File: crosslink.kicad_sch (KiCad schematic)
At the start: 32 parts, among them U16 CrossLink_LIF-MD6000-6JMG80I

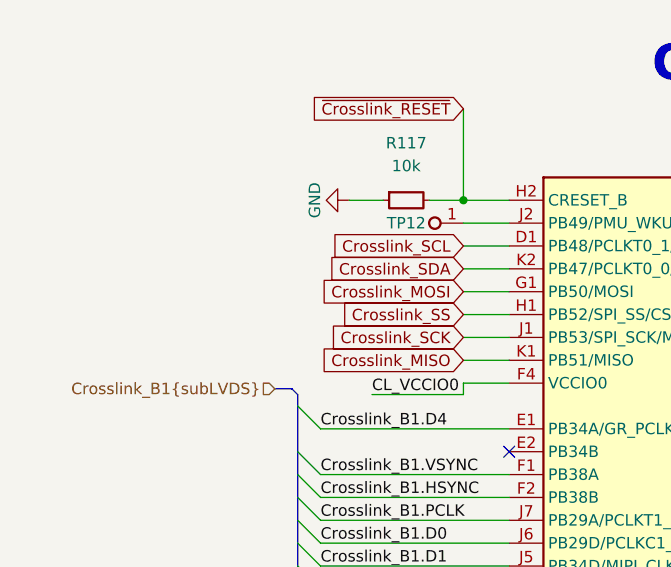
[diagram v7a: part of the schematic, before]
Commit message: [#57505] Start moving logic level converters to GPIO sheet
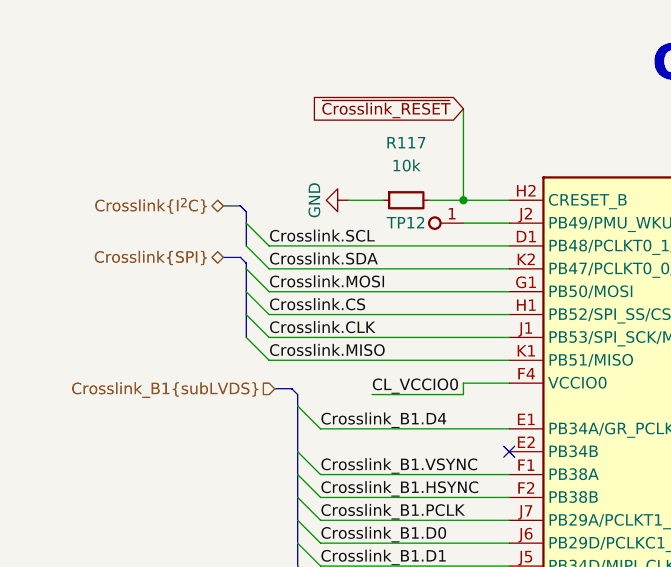
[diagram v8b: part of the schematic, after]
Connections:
- net Crosslink_MISO renamed Crosslink.MISO
- net Crosslink_MOSI renamed Crosslink.MOSI
- net Crosslink_SCK renamed Crosslink.CLK
- net Crosslink_SCL renamed Crosslink.SCL
- net Crosslink_SDA renamed Crosslink.SDA
- net Crosslink_SS renamed Crosslink.CS
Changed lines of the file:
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@@
     (stroke (width 0) (type default))
   )
+  (bus_entry (at 39.37 90.805) (size -2.54 -2.54)
+    (stroke (width 0) (type default))
+  )
   (bus_entry (at 42.545 141.605) (size 2.54 2.54)
     (stroke (width 0) (type default))
@@
     (stroke (width 0) (type default))
   )
+  (bus_entry (at 39.37 103.505) (size -2.54 -2.54)
+    (stroke (width 0) (type default))
+  )
   (bus_entry (at 149.225 139.065) (size -2.54 2.54)
     (stroke (width 0) (type default))
@@
     (stroke (width 0) (type default))
   )
+  (bus_entry (at 39.37 100.965) (size -2.54 -2.54)
+    (stroke (width 0) (type default))
+  )
   (bus_entry (at 149.225 136.525) (size -2.54 2.54)
     (stroke (width 0) (type default))
@@
     (stroke (width 0) (type default))
   )
+  (bus_entry (at 39.37 98.425) (size -2.54 -2.54)
+    (stroke (width 0) (type default))
+  )
   (bus_entry (at 149.225 156.845) (size -2.54 2.54)
     (stroke (width 0) (type default))
@@
     (stroke (width 0) (type default))
   )
+  (bus_entry (at 39.37 95.885) (size -2.54 -2.54)
+    (stroke (width 0) (type default))
+  )
   (bus_entry (at 42.545 116.205) (size 2.54 2.54)
     (stroke (width 0) (type default))
@@
     (stroke (width 0) (type default))
   )
+  (bus_entry (at 39.37 93.345) (size -2.54 -2.54)
+    (stroke (width 0) (type default))
+  )
   (bus_entry (at 42.545 184.785) (size 2.54 2.54)
     (stroke (width 0) (type default))
@@
     (stroke (width 0) (type default))
   )
-  (wire (pts (xy 60.96 93.345) (xy 66.04 93.345))
+  (wire (pts (xy 39.37 93.345) (xy 66.04 93.345))
+    (stroke (width 0) (type default))
+  )
+  (bus (pts (xy 36.83 98.425) (xy 36.83 100.965))
     (stroke (width 0) (type default))
   )
@@
     (stroke (width 0) (type default))
   )
+  (bus (pts (xy 36.83 95.885) (xy 36.83 98.425))
+    (stroke (width 0) (type default))
+  )
   (wire (pts (xy 129.54 111.125) (xy 146.685 111.125))
     (stroke (width 0) (type default))
@@
     (stroke (width 0) (type default))
   )
+  (bus (pts (xy 36.83 88.265) (xy 36.83 90.805))
+    (stroke (width 0) (type default))
+  )
   (wire (pts (xy 304.8 101.6) (xy 311.15 101.6))
     (stroke (width 0) (type default))
@@
     (stroke (width 0) (type default))
   )
-  (wire (pts (xy 60.96 103.505) (xy 66.04 103.505))
+  (wire (pts (xy 39.37 103.505) (xy 66.04 103.505))
     (stroke (width 0) (type default))
   )
@@
     (stroke (width 0) (type default))
   )
+  (bus (pts (xy 34.29 86.36) (xy 36.195 86.36))
+    (stroke (width 0) (type default))
+  )
+  (bus (pts (xy 36.195 92.075) (xy 36.83 92.71))
+    (stroke (width 0) (type default))
+  )
+  (bus (pts (xy 36.195 86.36) (xy 36.83 86.995))
+    (stroke (width 0) (type default))
+  )
   (bus (pts (xy 149.86 133.35) (xy 149.225 133.985))
     (stroke (width 0) (type default))
@@
     (stroke (width 0) (type default))
   )
+  (bus (pts (xy 36.83 86.995) (xy 36.83 88.265))
+    (stroke (width 0) (type default))
+  )
   (wire (pts (xy 45.085 118.745) (xy 66.04 118.745))
     (stroke (width 0) (type default))
@@
     (stroke (width 0) (type default))
   )
-  (wire (pts (xy 60.96 95.885) (xy 66.04 95.885))
+  (wire (pts (xy 39.37 95.885) (xy 66.04 95.885))
     (stroke (width 0) (type default))
   )
@@
     (stroke (width 0) (type default))
   )
-  (wire (pts (xy 60.96 98.425) (xy 66.04 98.425))
+  (wire (pts (xy 39.37 98.425) (xy 66.04 98.425))
     (stroke (width 0) (type default))
   )
@@
     (stroke (width 0) (type default))
   )
-  (wire (pts (xy 60.96 90.805) (xy 66.04 90.805))
+  (wire (pts (xy 39.37 90.805) (xy 66.04 90.805))
     (stroke (width 0) (type default))
   )
@@
     (stroke (width 0) (type default))
   )
+  (bus (pts (xy 36.83 92.71) (xy 36.83 93.345))
+    (stroke (width 0) (type default))
+  )
+  (bus (pts (xy 34.29 92.075) (xy 36.195 92.075))
+    (stroke (width 0) (type default))
+  )
   (bus (pts (xy 149.225 113.665) (xy 149.225 116.205))
     (stroke (width 0) (type default))
@@
     (stroke (width 0) (type default))
   )
+  (bus (pts (xy 36.83 93.345) (xy 36.83 95.885))
+    (stroke (width 0) (type default))
+  )
   (wire (pts (xy 345.44 93.98) (xy 355.6 93.98))
     (stroke (width 0) (type default))
@@
     (stroke (width 0) (type default))
   )
-  (wire (pts (xy 60.96 100.965) (xy 66.04 100.965))
+  (wire (pts (xy 39.37 100.965) (xy 66.04 100.965))
     (stroke (width 0) (type default))
   )
@@
     (effects (font (size 1.27 1.27)) (justify right bottom))
   )
+  (label "Crosslink.CS" (at 39.37 98.425 0) (fields_autoplaced)
+    (effects (font (size 1.27 1.27)) (justify left bottom))
+  )
   (label "Crosslink_B2.D8" (at 45.085 189.865 0) (fields_autoplaced)
     (effects (font (size 1.27 1.27)) (justify left bottom))
@@
     (effects (font (size 1.27 1.27)) (justify right bottom))
   )
+  (label "Crosslink.SDA" (at 39.37 93.345 0) (fields_autoplaced)
+    (effects (font (size 1.27 1.27)) (justify left bottom))
+  )
   (label "DSI1.D2_N" (at 145.415 156.845 180) (fields_autoplaced)
     (effects (font (size 1.27 1.27)) (justify right bottom))
@@
     (effects (font (size 1.27 1.27)) (justify left bottom))
   )
+  (label "Crosslink.MISO" (at 39.37 103.505 0) (fields_autoplaced)
+    (effects (font (size 1.27 1.27)) (justify left bottom))
+  )
   (label "CAM1.C_N" (at 145.415 103.505 180) (fields_autoplaced)
     (effects (font (size 1.27 1.27)) (justify right bottom))
@@
     (effects (font (size 1.27 1.27)) (justify right bottom))
   )
+  (label "Crosslink.SCL" (at 39.37 90.805 0) (fields_autoplaced)
+    (effects (font (size 1.27 1.27)) (justify left bottom))
+  )
   (label "DSI1.C_N" (at 145.415 141.605 180) (fields_autoplaced)
     (effects (font (size 1.27 1.27)) (justify right bottom))
   )
+  (label "Crosslink.MOSI" (at 39.37 95.885 0) (fields_autoplaced)
+    (effects (font (size 1.27 1.27)) (justify left bottom))
+  )
   (label "Crosslink_B1.D9" (at 45.085 144.145 0) (fields_autoplaced)
     (effects (font (size 1.27 1.27)) (justify left bottom))
@@
     (effects (font (size 1.27 1.27)) (justify left bottom))
   )
+  (label "Crosslink.CLK" (at 39.37 100.965 0) (fields_autoplaced)
+    (effects (font (size 1.27 1.27)) (justify left bottom))
+  )
   (label "Crosslink_B1.D4" (at 45.085 111.125 0) (fields_autoplaced)
     (effects (font (size 1.27 1.27)) (justify left bottom))
@@
     (effects (font (size 1.27 1.27)) (justify right bottom))
   )
-  (global_label "Crosslink_SCL" (shape input) (at 60.96 90.805 180) (fields_autoplaced)
-    (effects (font (size 1.27 1.27)) (justify right))
-    (property "Intersheetrefs" "${INTERSHEET_REFS}" (at 45.3631 90.7256 0)
-      (effects (font (size 1.27 1.27)) (justify right))
-    )
-  )
-  (global_label "Crosslink_SCK" (shape input) (at 60.96 100.965 180) (fields_autoplaced)
-    (effects (font (size 1.27 1.27)) (justify right))
-    (property "Intersheetrefs" "${INTERSHEET_REFS}" (at 45.1212 100.8856 0)
-      (effects (font (size 1.27 1.27)) (justify right))
-    )
-  )
-  (global_label "Crosslink_SDA" (shape input) (at 60.96 93.345 180) (fields_autoplaced)
-    (effects (font (size 1.27 1.27)) (justify right))
-    (property "Intersheetrefs" "${INTERSHEET_REFS}" (at 45.3026 93.2656 0)
-      (effects (font (size 1.27 1.27)) (justify right))
-    )
-  )
-  (global_label "Crosslink_SS" (shape input) (at 60.96 98.425 180) (fields_autoplaced)
-    (effects (font (size 1.27 1.27)) (justify right))
-    (property "Intersheetrefs" "${INTERSHEET_REFS}" (at 46.4517 98.3456 0)
-      (effects (font (size 1.27 1.27)) (justify right))
-    )
-  )
-  (global_label "Crosslink_MOSI" (shape input) (at 60.96 95.885 180) (fields_autoplaced)
-    (effects (font (size 1.27 1.27)) (justify right))
-    (property "Intersheetrefs" "${INTERSHEET_REFS}" (at 44.2745 95.8056 0)
-      (effects (font (size 1.27 1.27)) (justify right))
-    )
-  )
   (global_label "1V8_CL" (shape input) (at 281.94 93.98 180) (fields_autoplaced)
     (effects (font (size 1.27 1.27)) (justify right))
@@
     )
   )
-  (global_label "Crosslink_MISO" (shape input) (at 60.96 103.505 180) (fields_autoplaced)
-    (effects (font (size 1.27 1.27)) (justify right))
-    (property "Intersheetrefs" "${INTERSHEET_REFS}" (at 44.2745 103.4256 0)
-      (effects (font (size 1.27 1.27)) (justify right))
-    )
-  )
   (global_label "2V5_CL" (shape input) (at 241.3 129.54 180) (fields_autoplaced)
     (effects (font (size 1.27 1.27)) (justify right))
@@
     (effects (font (size 1.27 1.27)) (justify right))
   )
+  (hierarchical_label "Crosslink{SPI}" (shape bidirectional) (at 34.29 92.075 180) (fields_autoplaced)
+    (effects (font (size 1.27 1.27)) (justify right))
+  )
   (hierarchical_label "DSI1{DSI}" (shape bidirectional) (at 151.765 133.35 0) (fields_autoplaced)
     (effects (font (size 1.27 1.27)) (justify left))
@@
     (effects (font (size 1.27 1.27)) (justify left))
   )
+  (hierarchical_label "Crosslink{I^{2}C}" (shape bidirectional) (at 34.29 86.36 180) (fields_autoplaced)
+    (effects (font (size 1.27 1.27)) (justify right))
+  )
   (symbol (lib_id "antmicropower:GND") (at 361.95 120.65 0) (unit 1)
